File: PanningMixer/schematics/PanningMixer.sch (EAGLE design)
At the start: 86 parts, among them IC1 NE5532D, IC2 NE5532D, IC3 TL072D, IC4 TL072D, J1 CON-JST_PH_3W, J2 CON-JST_PH_3W, Q1 BSS84, Q2 BSS123, U1 CON-PROSIGNAL_MJ-355W, U2 CON-JST_PH_5W, U4 CON-JST_PH_5W

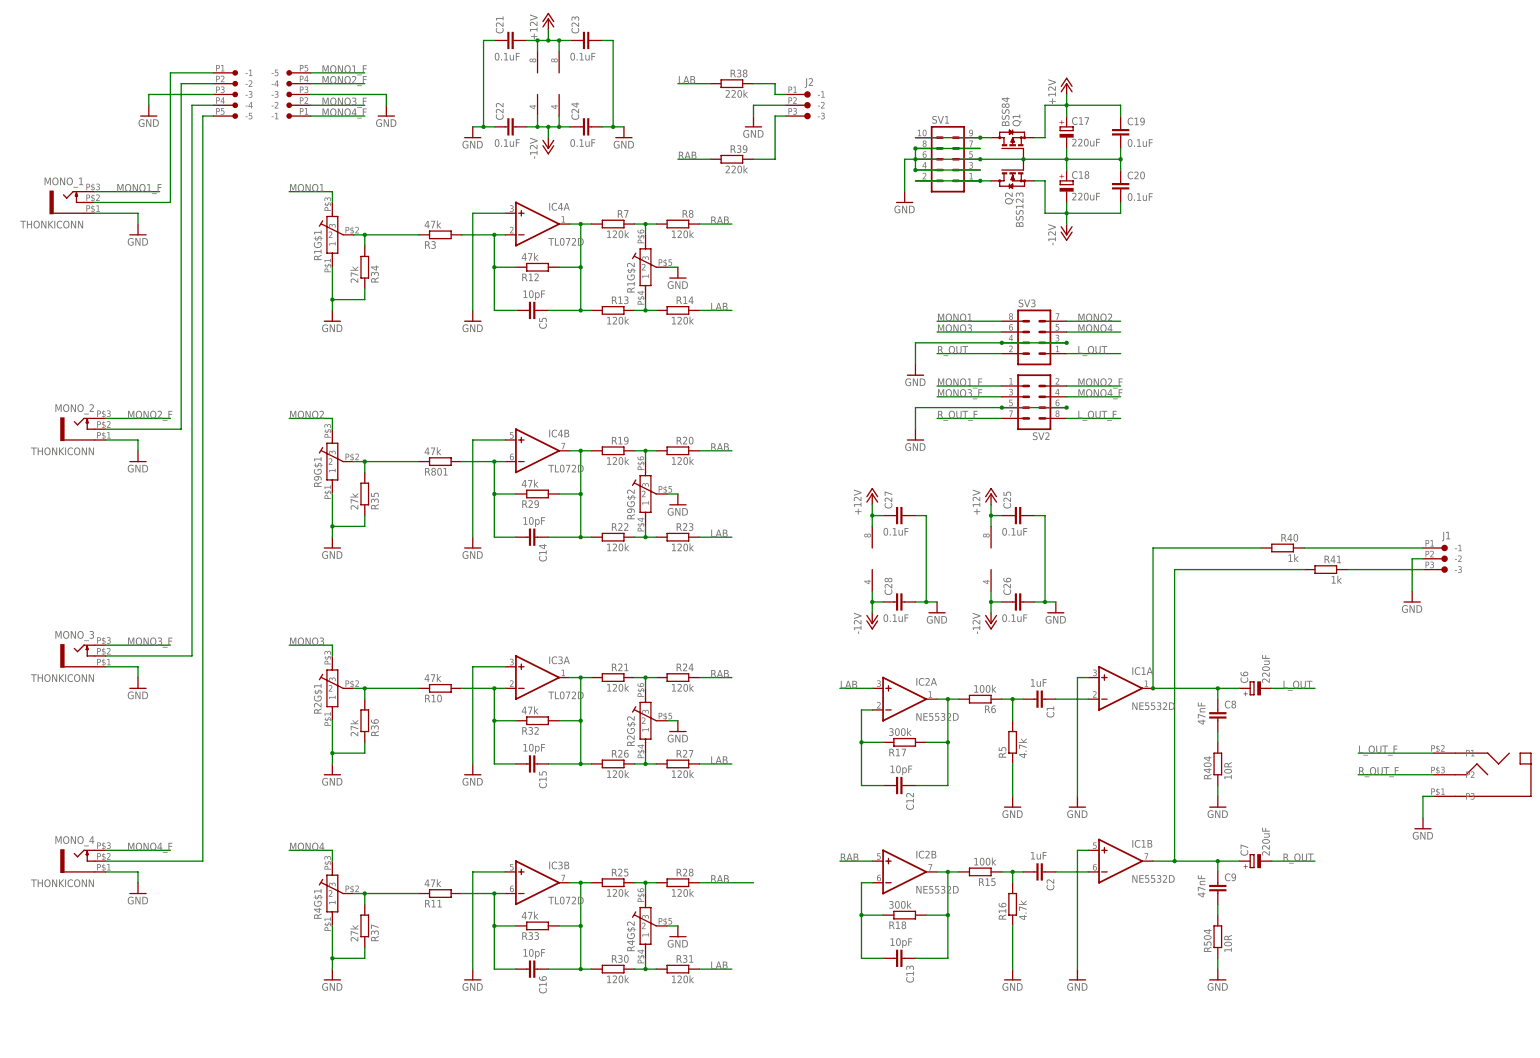
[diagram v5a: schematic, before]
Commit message: changed hp amplifier stage, joined up ground planes
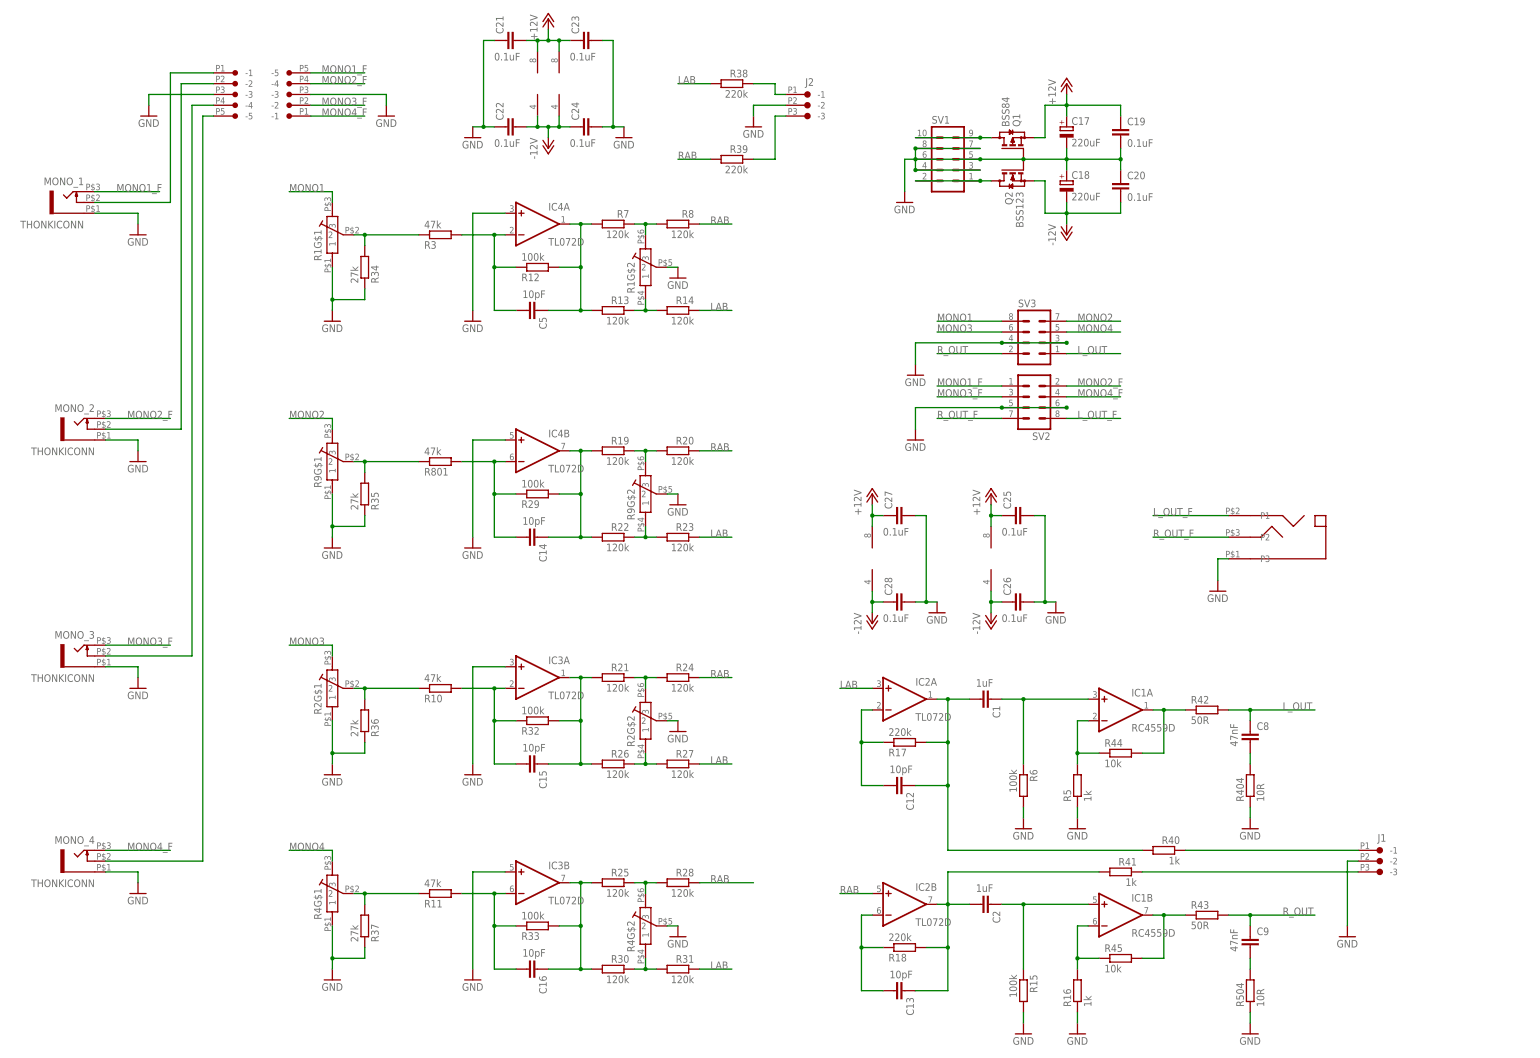
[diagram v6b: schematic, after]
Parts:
- removed C6, C7: 220uF, rcl:CPOL-EUA
- added R42, R43: 50R, Rebel:R-EU_0603
- added R44, R45: 10k, Rebel:R-EU_0603
- IC1: value NE5532D -> RC4559D; device linear:NE5532D -> linear:RC4559D
- IC2: value NE5532D -> TL072D; device linear:NE5532D -> linear:TL072D
- R12, R29, R32, R33: value 47k -> 100k
- R16, R5: value 4.7k -> 1k
- R17, R18: value 300k -> 220k
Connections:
- removed net N$13: C12.1, IC2A.OUT, R17.2, R6.2
- removed net N$18: C13.1, IC2B.OUT, R15.2, R18.2
- new net N$27: IC1A.OUT, R42.1, R44.2
- new net N$31: IC1B.OUT, R43.1, R45.2
- net GND: now also R15.2, R6.2; no longer IC1A.+IN, IC1B.+IN
- net L_OUT: now also C8.1, R42.2; no longer C6.-
- net N$22: now also C2.1, IC1B.+IN, R15.1; no longer C6.+, C8.1, IC1A.OUT, R40.2
- net N$28: now also IC1B.-IN, R16.2, R45.1; no longer C1.1, IC1A.-IN
- net N$29: now also C1.2, C12.1, IC2A.OUT, R17.2, R40.2; no longer C2.1, IC1B.-IN
- net N$3: now also C13.1, C2.2, IC2B.OUT, R18.2; no longer C7.+, C9.1, IC1B.OUT
- net N$5: now also C1.1, IC1A.+IN, R6.1; no longer C2.2, R15.1, R16.2
- net N$7: now also IC1A.-IN, R44.1; no longer C1.2, R6.1
- net R_OUT: now also C9.1, R43.2; no longer C7.-
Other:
- moved on the sheet: C1, C13, C2, C8, C9, IC1A, IC1B, IC2B, J1, R15, R16, R18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

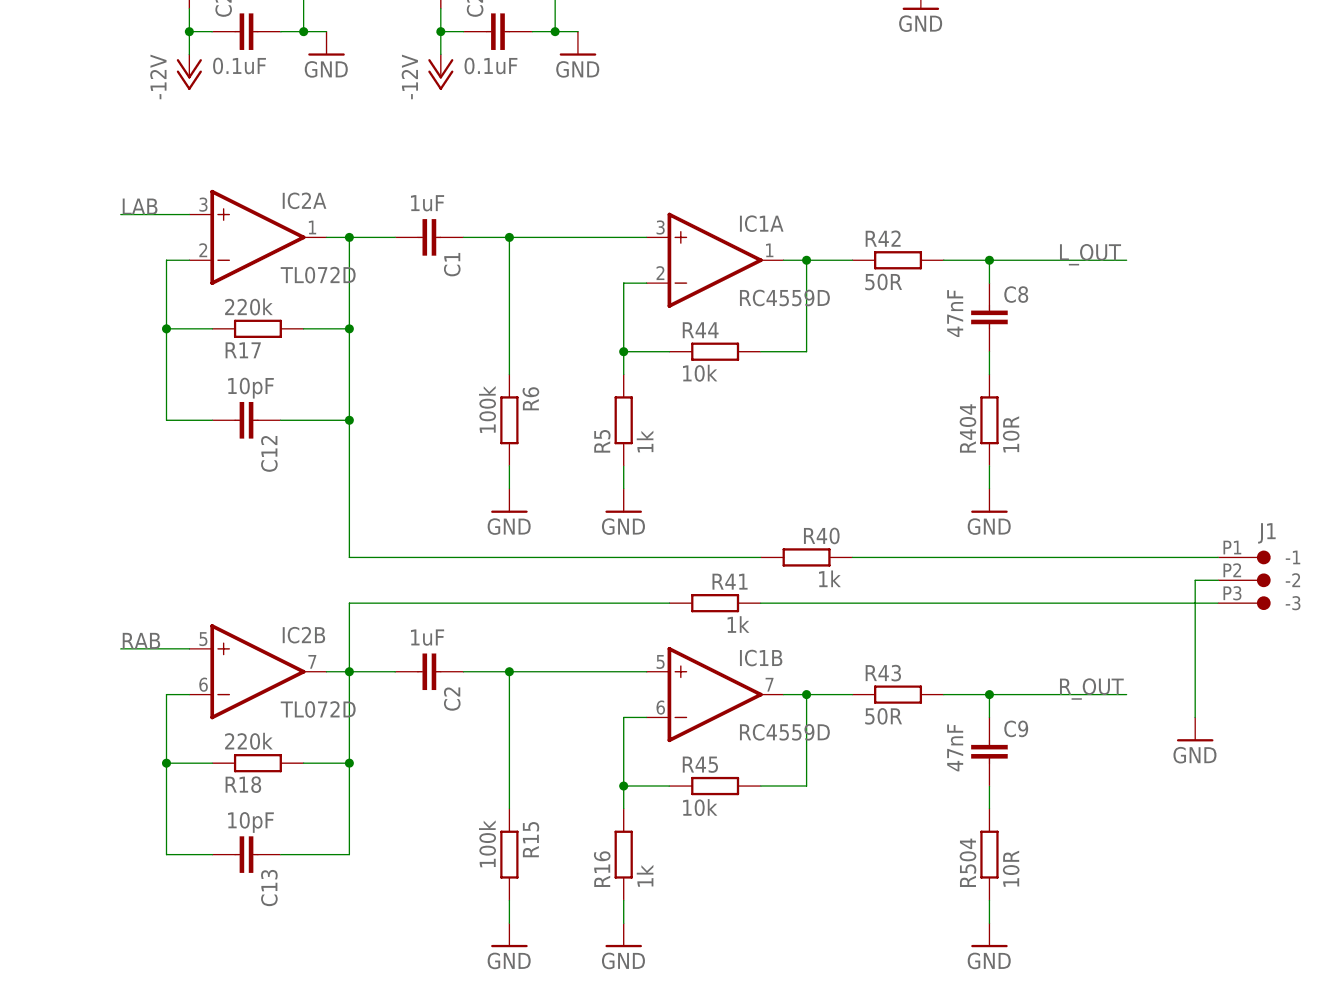
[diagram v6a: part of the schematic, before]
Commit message: changed to inverting hp amp, simple summing buffer.
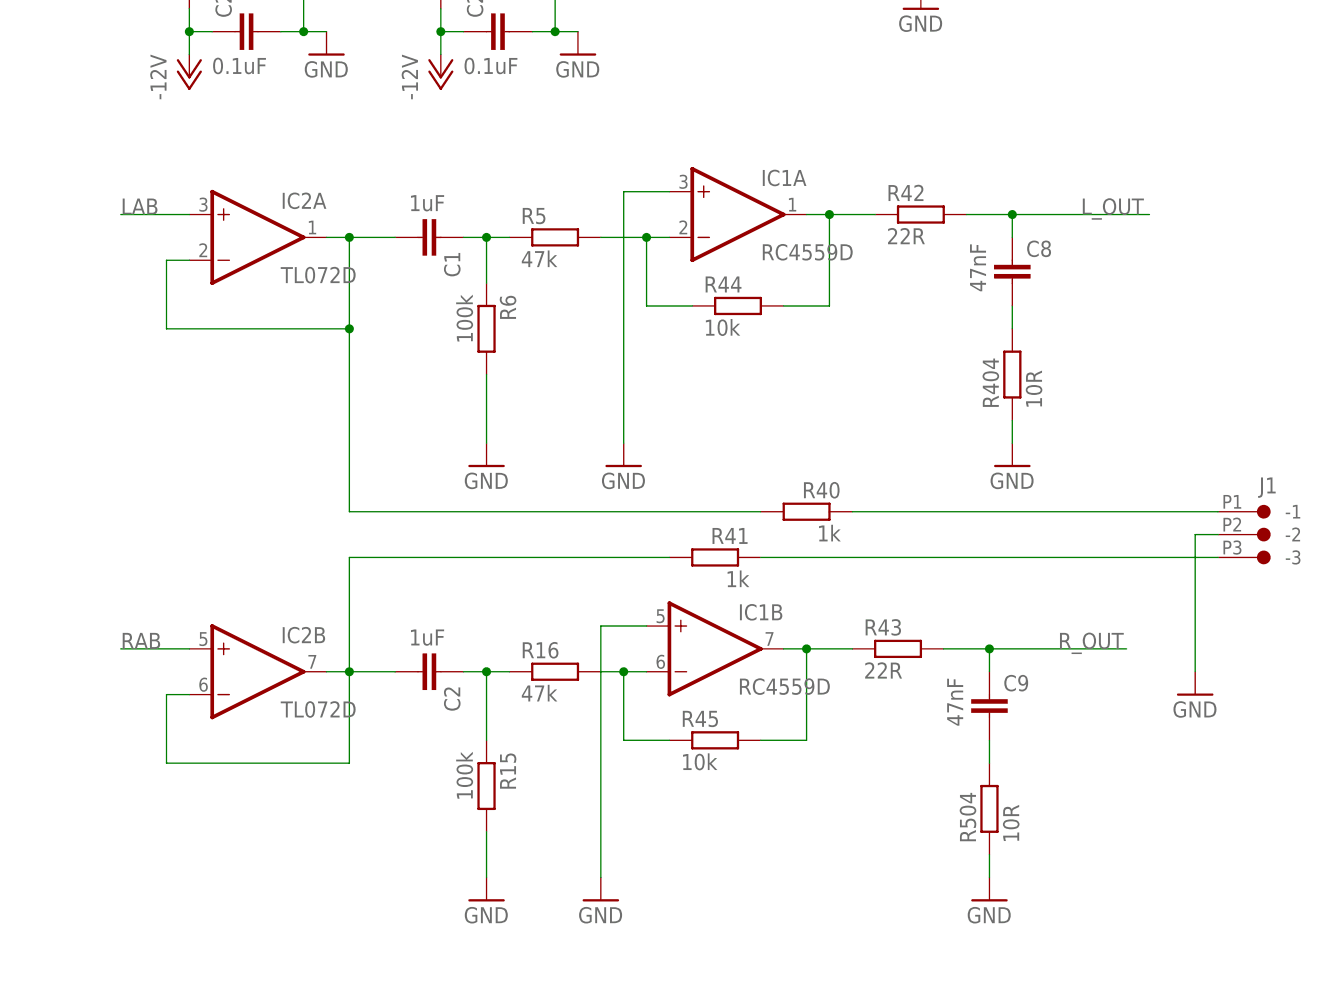
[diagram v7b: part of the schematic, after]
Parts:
- removed C12, C13: 10pF, Rebel:C-EUC0603
- removed R17, R18: 220k, Rebel:R-EU_0603
- R16, R5: value 1k -> 47k
- R42, R43: value 50R -> 22R
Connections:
- removed net N$29: C1.2, C12.1, IC2A.OUT, R17.2, R40.2
- removed net N$3: C13.1, C2.2, IC2B.OUT, R18.2, R41.2
- net GND: now also IC1A.+IN, IC1B.+IN; no longer R16.1, R5.1
- net N$22: now also R16.1; no longer IC1B.+IN
- net N$30: now also C1.2, IC2A.OUT, R40.2; no longer C12.2, R17.1
- net N$32: now also C2.2, IC2B.OUT, R41.2; no longer C13.2, R18.1
- net N$5: now also R5.1; no longer IC1A.+IN
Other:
- moved on the sheet: C8, C9, IC1A, IC1B, J1, R15, R16, R40, R404, R41, R42, R43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

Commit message: updated all resistors to Rebel R0603, slimmed boardsize, minor routing
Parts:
- R15, R16, R404, R5, R504, R6: device resistor:R-EU_R0603 -> Rebel:R-EU_0603
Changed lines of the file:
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@@
 </classes>
 <parts>
-<part name="R404" library="resistor" deviceset="R-EU_" device="R0603" value="10R"/>
+<part name="R404" library="Rebel" deviceset="R-EU_" device="0603" value="10R"/>
 <part name="MONO_3" library="Rebel" deviceset="THONKICONN" device=""/>
-<part name="R504" library="resistor" deviceset="R-EU_" device="R0603" value="10R"/>
+<part name="R504" library="Rebel" deviceset="R-EU_" device="0603" value="10R"/>
 <part name="MONO_4" library="Rebel" deviceset="THONKICONN" device=""/>
 <part name="P-7" library="supply1" deviceset="-12V" device=""/>
@@
 <part name="P-2" library="supply1" deviceset="-12V" device=""/>
 <part name="GND11" library="supply1" deviceset="GND" device=""/>
-<part name="R5" library="resistor" deviceset="R-EU_" device="R0603" value="47k"/>
-<part name="R6" library="resistor" deviceset="R-EU_" device="R0603" value="100k"/>
-<part name="R15" library="resistor" deviceset="R-EU_" device="R0603" value="100k"/>
-<part name="R16" library="resistor" deviceset="R-EU_" device="R0603" value="47k"/>
+<part name="R5" library="Rebel" deviceset="R-EU_" device="0603" value="47k"/>
+<part name="R6" library="Rebel" deviceset="R-EU_" device="0603" value="100k"/>
+<part name="R15" library="Rebel" deviceset="R-EU_" device="0603" value="100k"/>
+<part name="R16" library="Rebel" deviceset="R-EU_" device="0603" value="47k"/>
 <part name="GND8" library="supply1" deviceset="GND" device=""/>
 <part name="GND12" library="supply1" deviceset="GND" device=""/>
